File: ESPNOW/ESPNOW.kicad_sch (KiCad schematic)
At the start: 34 parts, among them J10 Conn_01x03_Pin, J11 Conn_01x03_Pin, J12 Conn_01x03_Pin, J13 Conn_01x03_Pin, J14 Screw_Terminal_01x02, J2 Screw_Terminal_01x14, J3 Conn_01x03_Pin, J4 Screw_Terminal_01x02, J5 Screw_Terminal_01x02, J6 Conn_01x03_Pin, J7 Conn_01x03_Pin, J8 Conn_01x03_Pin, J9 Conn_01x03_Pin, U4 TPS564255

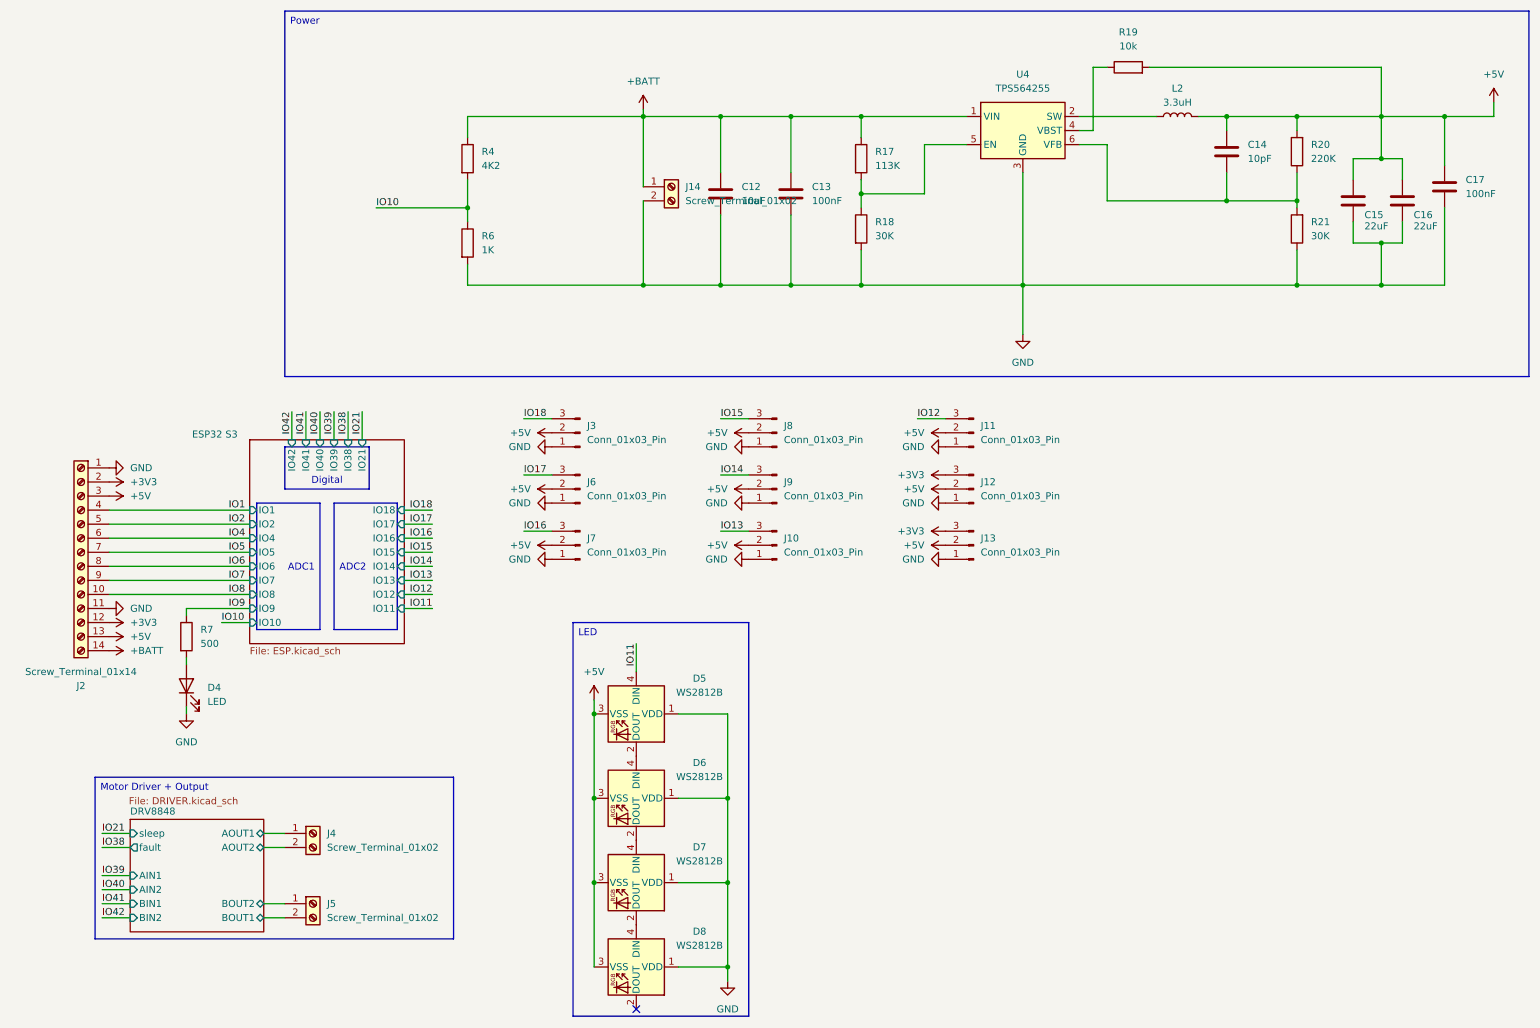
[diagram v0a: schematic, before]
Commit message: Third Iteration
Reworked general layout to reduce size

Reworked Motor Driver routing to comply with layout guidelines in datasheet

Reworked Buck Converter routing to comply with layout guidelines in datasheet

TODO:
Add info to back layer
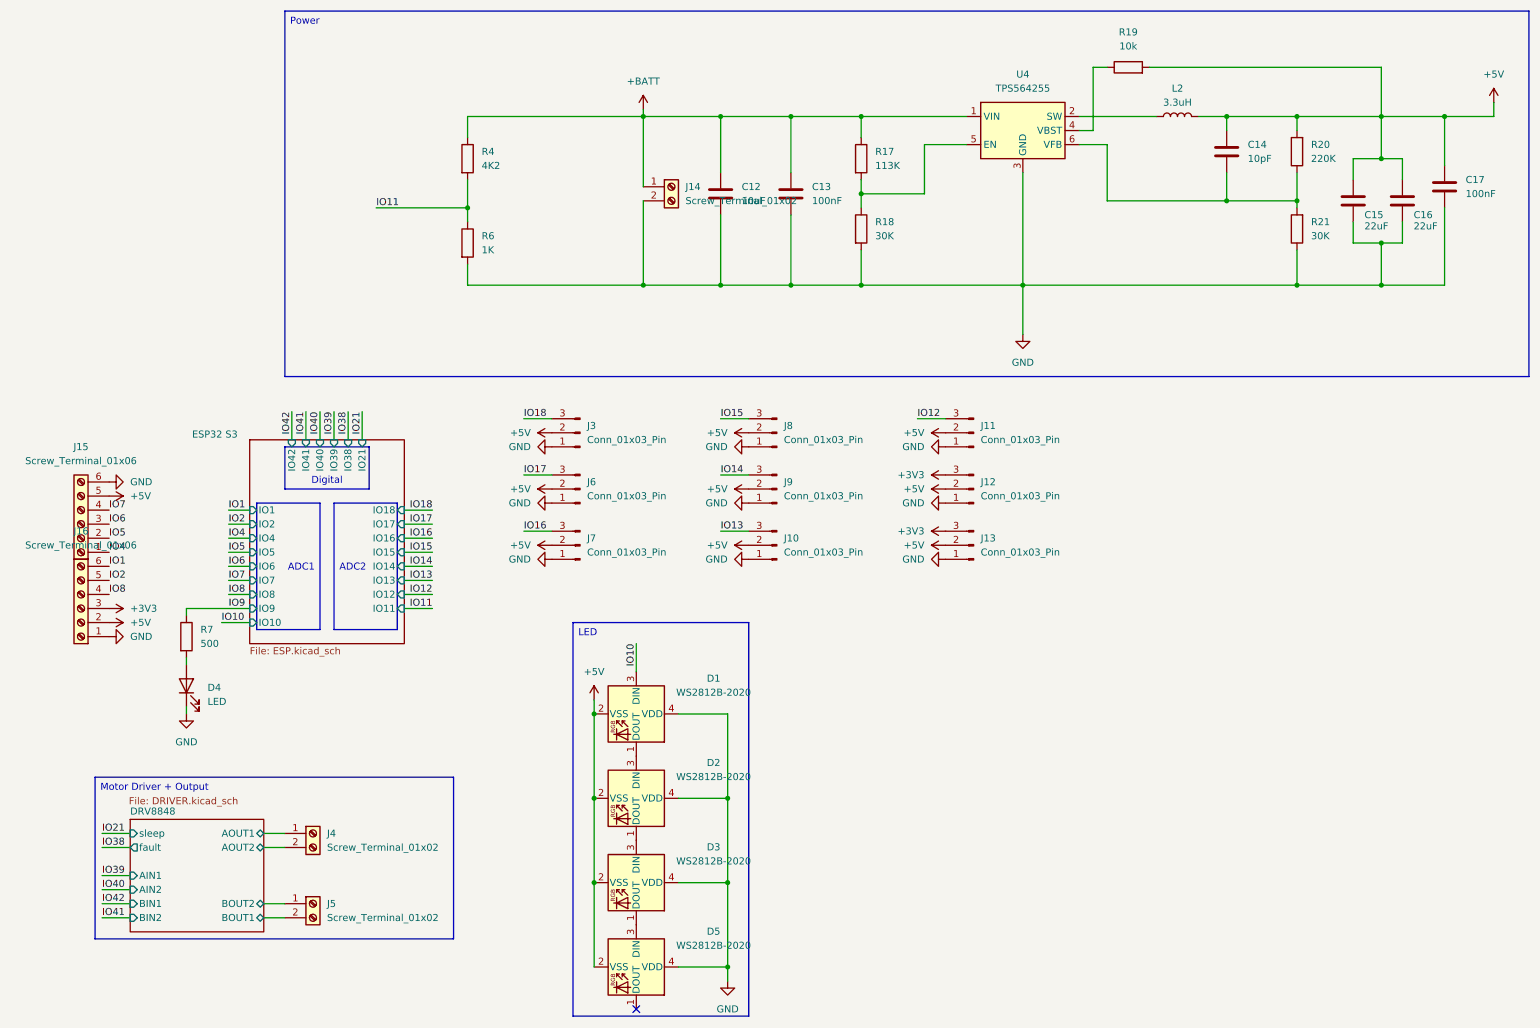
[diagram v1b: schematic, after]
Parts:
- removed D5, D6, D7, D8: WS2812B, LED_SMD:LED_WS2812B_PLCC4_5.0x5.0mm_P3.2mm, symbol LED:WS2812B
- removed J2: Screw_Terminal_01x14, TerminalBlock:TerminalBlock_MaiXu_MX126-5.0-14P_1x14_P5.00mm, symbol Connector:Screw_Terminal_01x14
- added D1, D2, D3, D5: WS2812B-2020, LED_SMD:LED_WS2812B-2020_PLCC4_2.0x2.0mm, symbol LED:WS2812B-2020
- added J15, J16: Screw_Terminal_01x06, TerminalBlock:TerminalBlock_MaiXu_MX126-5.0-06P_1x06_P5.00mm, symbol Connector:Screw_Terminal_01x06
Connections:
- net +3V3: now also J16.3 (Pin_3)
- net +5V: now also D1.2 (VSS), D2.2 (VSS), D3.2 (VSS), D5.2 (VSS), J15.5 (Pin_5), J16.2 (Pin_2)
- net GND: now also D1.4 (VDD), D2.4 (VDD), D3.4 (VDD), D5.4 (VDD), J15.6 (Pin_6), J16.1 (Pin_1)
- net IO1: now also J16.6 (Pin_6)
- net IO10: now also D1.3 (DIN); no longer R4.2, R6.1
- net IO11: now also R4.2, R6.1
- net IO2: now also J16.5 (Pin_5)
- net IO4: now also J15.1 (Pin_1)
- net IO5: now also J15.2 (Pin_2)
- net IO6: now also J15.3 (Pin_3)
- net IO7: now also J15.4 (Pin_4)
- net IO8: now also J16.4 (Pin_4)
- new net: D3.1 (DOUT), D5.3 (DIN)
- new net: D2.1 (DOUT), D3.3 (DIN)
- new net: D1.1 (DOUT), D2.3 (DIN)
